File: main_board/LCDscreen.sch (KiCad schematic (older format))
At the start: 12 parts

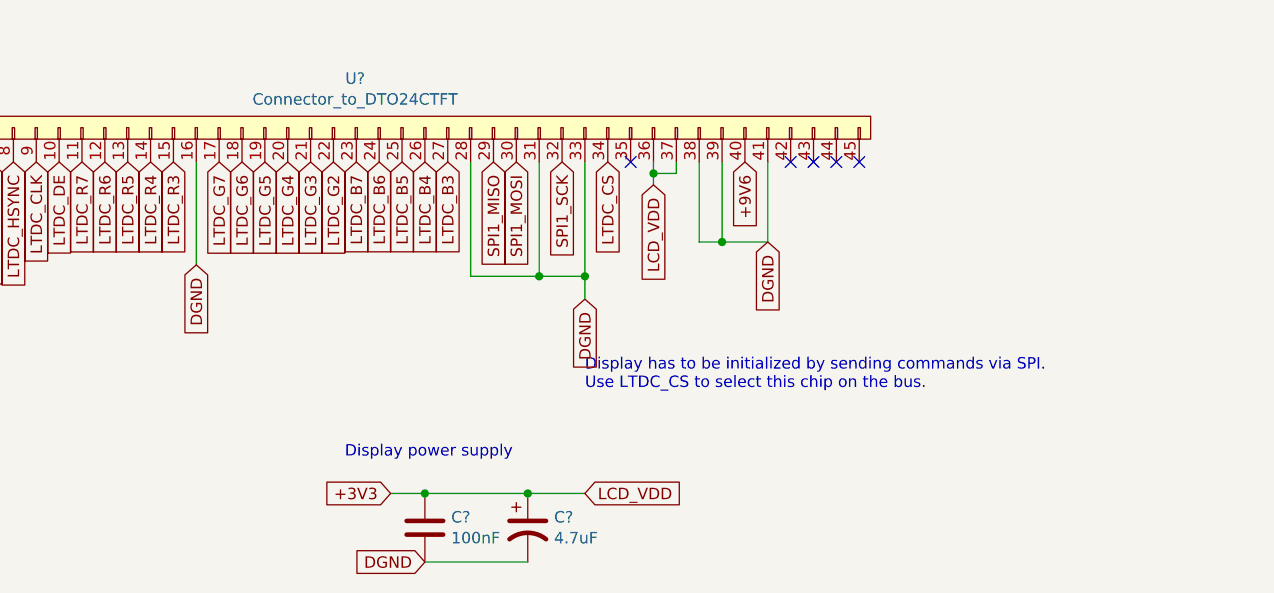
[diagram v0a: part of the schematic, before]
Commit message: Drew input and output audio stages in the schematic
Having trouble making hierarchical sheets refering to the same schematic file.
Could be a bug but also maybe I screwed up the schematic file
io_board/main_board_connector.sch because I changed the text in it to change
some global labels into hierarchical ones.
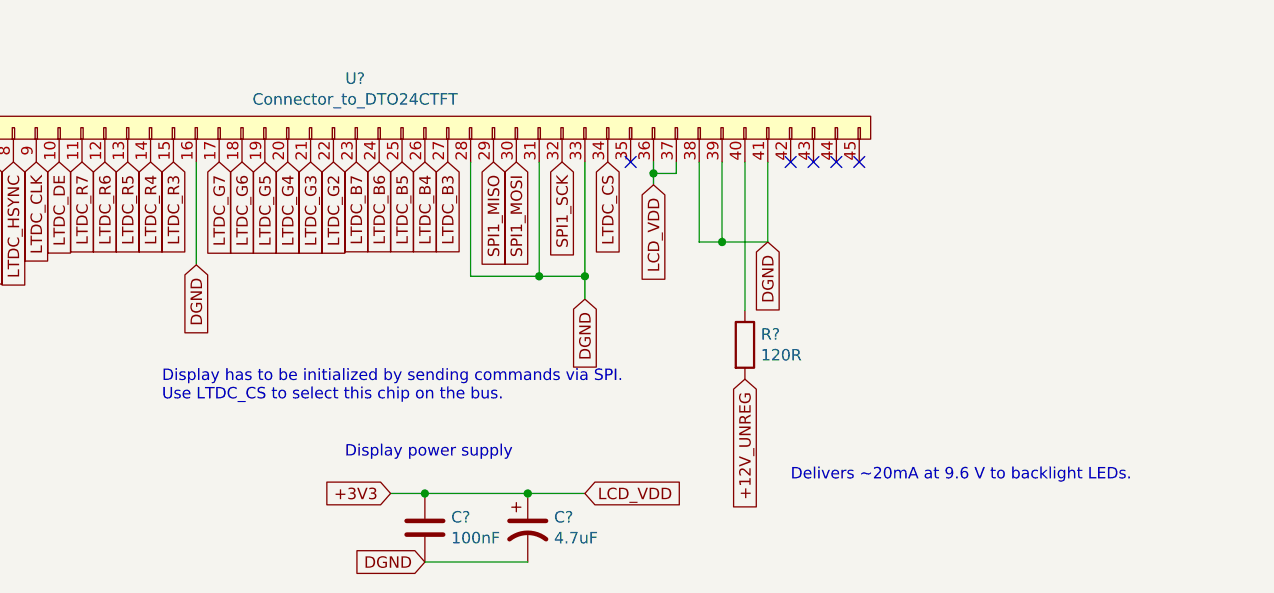
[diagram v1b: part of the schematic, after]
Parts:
- added R?: 120R, symbol Device:R
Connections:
- net +9V6: no longer names the net of U?.40
- net +9V6: now also R?.1
- new net +12V_UNREG: R?.2
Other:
- note added: "Delivers ~~20mA at 9.6 V to backlight LEDs."
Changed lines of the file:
@@
 EESchema Schematic File Version 4
-LIBS:midi_studio_v1-cache
+LIBS:main_board-cache
 EELAYER 26 0
 EELAYER END
@@
 NoConn ~ 9650 3350
 NoConn ~ 9550 3350
-Text GLabel 9350 3350 3    50   Input ~ 0
-+9V6
+Text GLabel 9350 4300 3    50   Input ~ 0
++12V_UNREG
 Wire Wire Line
 	9450 3350 9450 3700
@@
 Text GLabel 8750 3350 3    50   Input ~ 0
 LTDC_CS
-Text Notes 8650 4350 0    50   ~ 0
+Text Notes 6800 4400 0    50   ~ 0
 Display has to be initialized by sending commands via SPI.\nUse LTDC_CS to select this chip on the bus.
 Text GLabel 8250 3350 3    50   Input ~ 0
@@
 Text GLabel 8650 3950 3    50   Input ~ 0
 DGND
+$Comp
+L Device:R R?
+U 1 1 5D39FAE2
+P 9350 4150
+F 0 "R?" H 9420 4196 50  0000 L CNN
+F 1 "120R" H 9420 4105 50  0000 L CNN
+F 2 "" V 9280 4150 50  0001 C CNN
+F 3 "~" H 9350 4150 50  0001 C CNN
+	1    9350 4150
+	1    0    0    -1
+$EndComp
+Text Notes 9550 4750 0    50   ~ 0
+Delivers ~~20mA at 9.6 V to backlight LEDs.
+Wire Wire Line
+	9350 4000 9350 3350
 $EndSCHEMATC
